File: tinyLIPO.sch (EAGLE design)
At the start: 13 parts, among them IC1 MCP73831

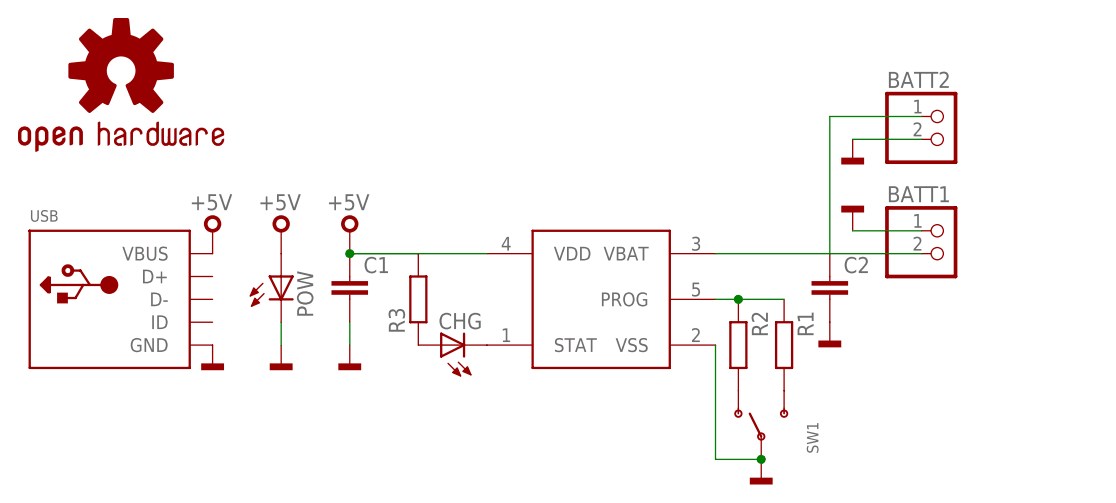
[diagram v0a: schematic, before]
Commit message: removed gerber schematic place adjustments added r4 r4,r3 from 220e to 470e board T.NAME adjust no DRC no ERC
Signed-off-by: kaushalpkk <kaushal.panduru@gmail.com>
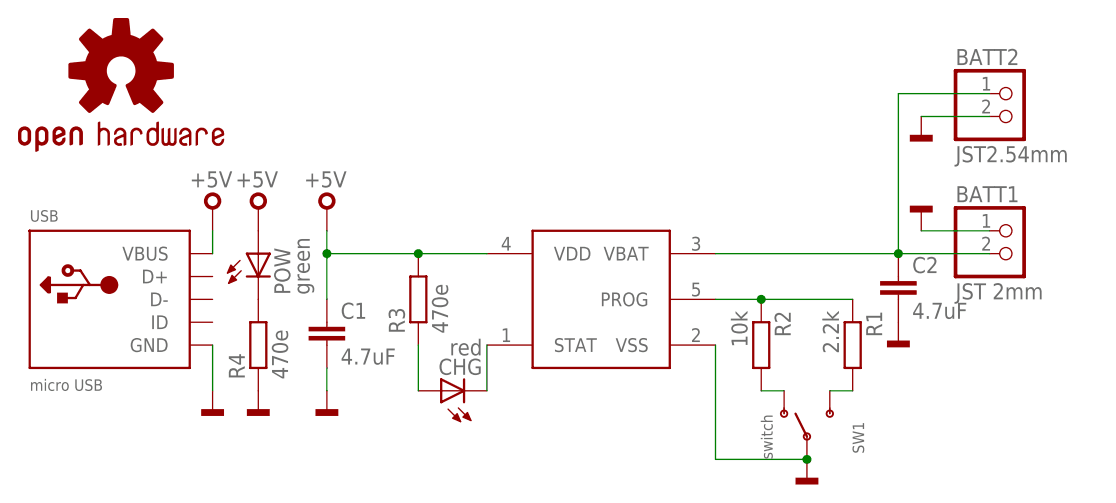
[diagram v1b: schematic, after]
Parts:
- added R4: 470e, rcl:R-EU_M0805
- BATT1: value (none) -> JST 2mm
- BATT2: value (none) -> JST2.54mm
- C1, C2: value (none) -> 4.7uF
- CHG: value (none) -> red
- POW: value (none) -> green
- R1: value (none) -> 2.2k
- R2: value (none) -> 10k
- R3: value (none) -> 470e
- SW1: value (none) -> switch
- USB: value (none) -> micro USB
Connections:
- new net N$7: POW.C, R4.2
- net GND: now also R4.1; no longer POW.C
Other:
- moved on the sheet: BATT1, BATT2, C1, C2, CHG, POW, R1, R2, SW1
